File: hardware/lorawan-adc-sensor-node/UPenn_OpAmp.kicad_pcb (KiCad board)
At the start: 2 copper layers, 106 x 147.1 mm, 61 parts, among them J1 643416-1, J2 Conn_02x03_Odd_Even, J3 Conn_01x13_Pin, J4 Conn_01x13_Pin, J5 Conn_02x03_Odd_Even, J6 643416-1, J7 643416-1, SW1 SW_DIP_x03, U1 AD8226, U2 AD8615, U3 ADP7142AUJZ-3.3, U4 AD8226, U5 AD8615, U6 AD8226, U7 AD8615

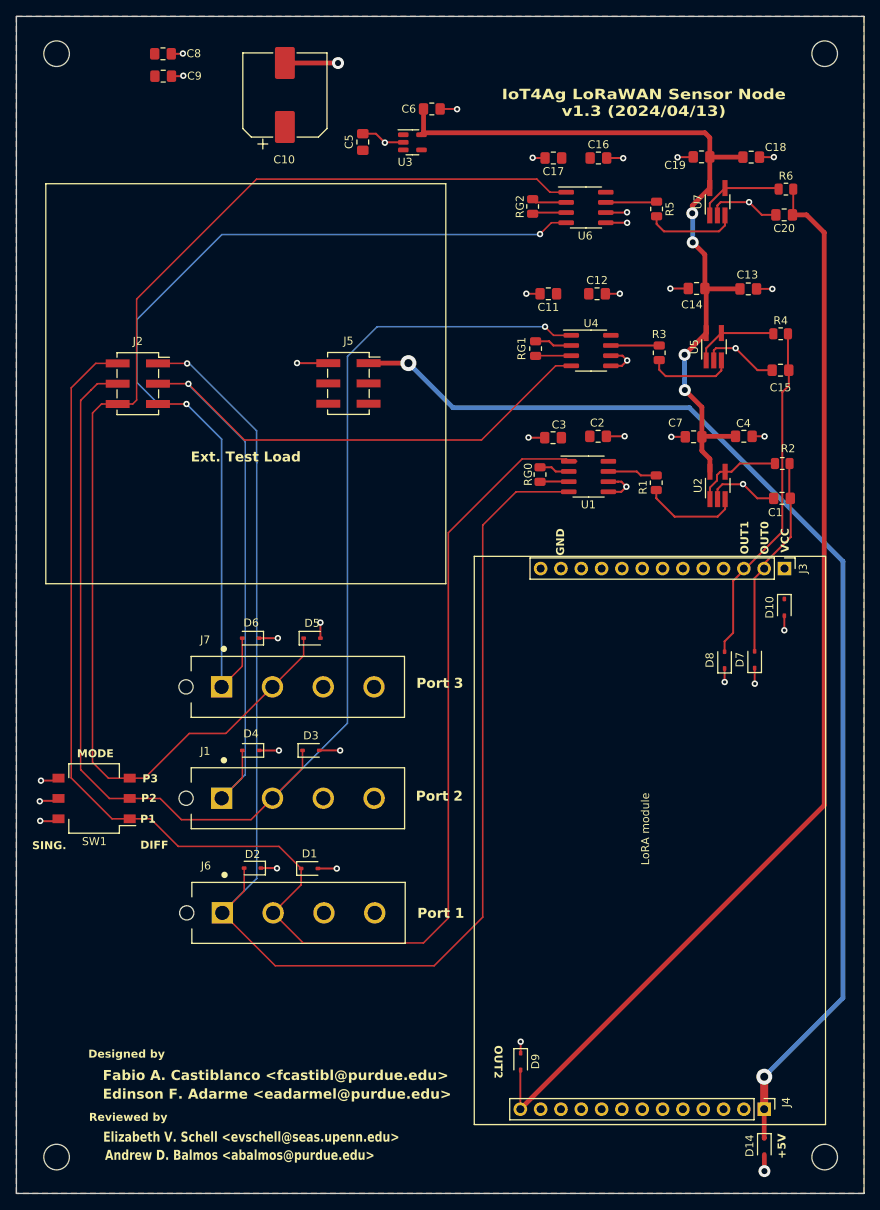
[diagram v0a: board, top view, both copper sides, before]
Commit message: fixed spacing between port connectors and minor layout cosmetic changes
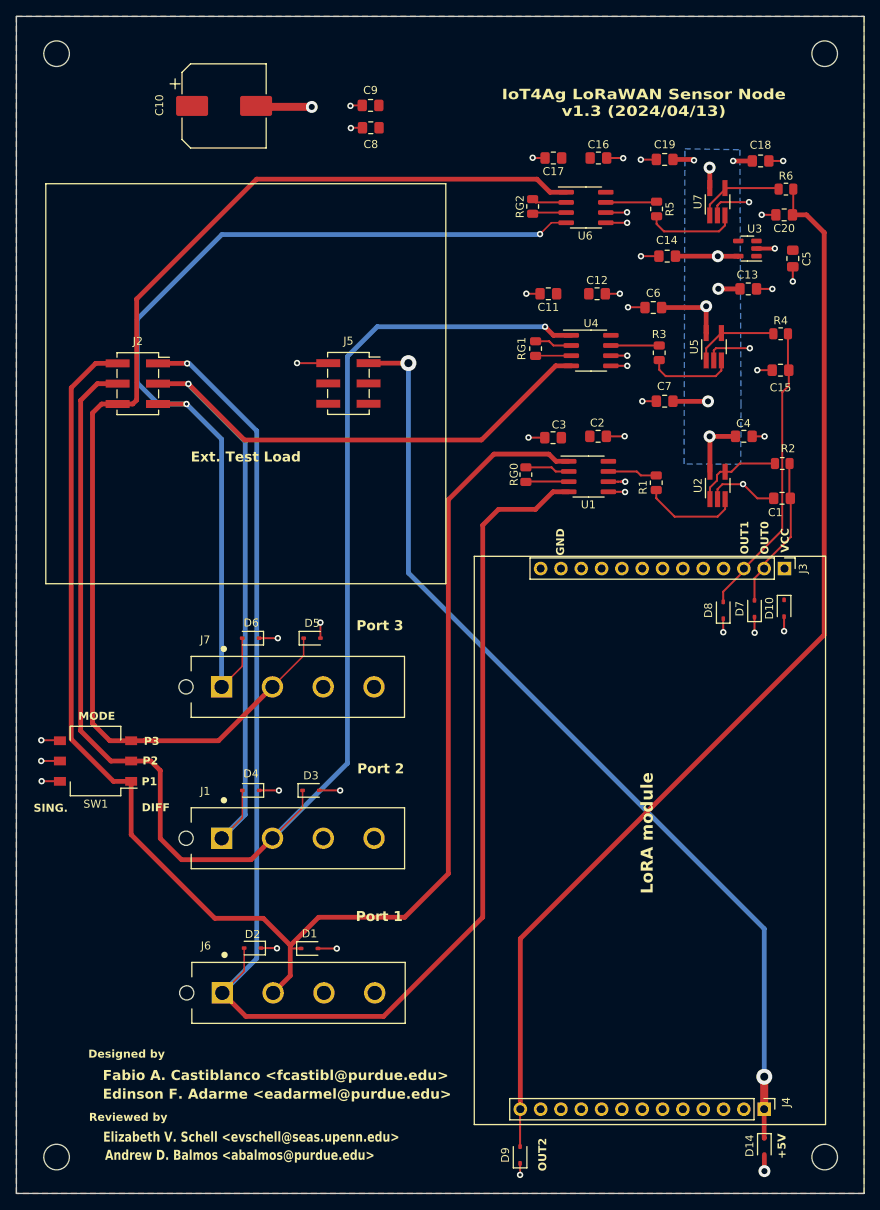
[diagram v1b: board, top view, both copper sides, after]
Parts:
- moved C5 55.7 mm to (149.8, 57.5), turned to 90 degrees
- moved U3 43.9 mm to (144.2, 56.2), turned to 180 degrees
- moved C6 37.2 mm to (132.4, 63.6), turned to 0 degrees
- moved C8 27.6 mm to (97.1, 41.1), turned to 180 degrees
- moved C9 26.2 mm to (97.1, 38.3), turned to 180 degrees
- moved D9 11.7 mm to (115.8, 169.5), turned to 90 degrees
- moved D1 10.0 mm to (89.4, 143.7)
- moved D2 10.0 mm to (82.3, 143.7)
- moved J6 10.0 mm to (88.1, 149.3)
- moved C10 7.72 mm to (78.8, 38.4), turned to 0 degrees
- moved D7 6.37 mm to (145.1, 101.2)
- moved D8 6.22 mm to (141.2, 101.4)
- moved C7 5.74 mm to (133.8, 75.3)
- moved C14 5.46 mm to (134.1, 57.2)
- moved D3 5.00 mm to (89.6, 124.0)
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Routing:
- net /VADC: track 98.3 -> 39.3 mm, vias 4 -> 8
- net /5V_SW: track 145.7 -> 120.3 mm
- net /P1+: track 183.9 -> 195.0 mm
- net /P2-: track 176.0 -> 185.2 mm
- net GND: track 116.8 -> 110.2 mm, vias 39 -> 44
- net /P3-: track 158.8 -> 152.3 mm
- net /P1_OUT: track 25.4 -> 19.1 mm
- net /P2_OUT: track 43.1 -> 37.0 mm
- net /P2+: track 121.5 -> 126.4 mm
- net /RG0-: track 3.59 -> 5.36 mm
- net /RG0+: track 3.81 -> 5.58 mm
- net /P1-: track 189.2 -> 190.2 mm
- added copper zone on B.Cu, net /VADC

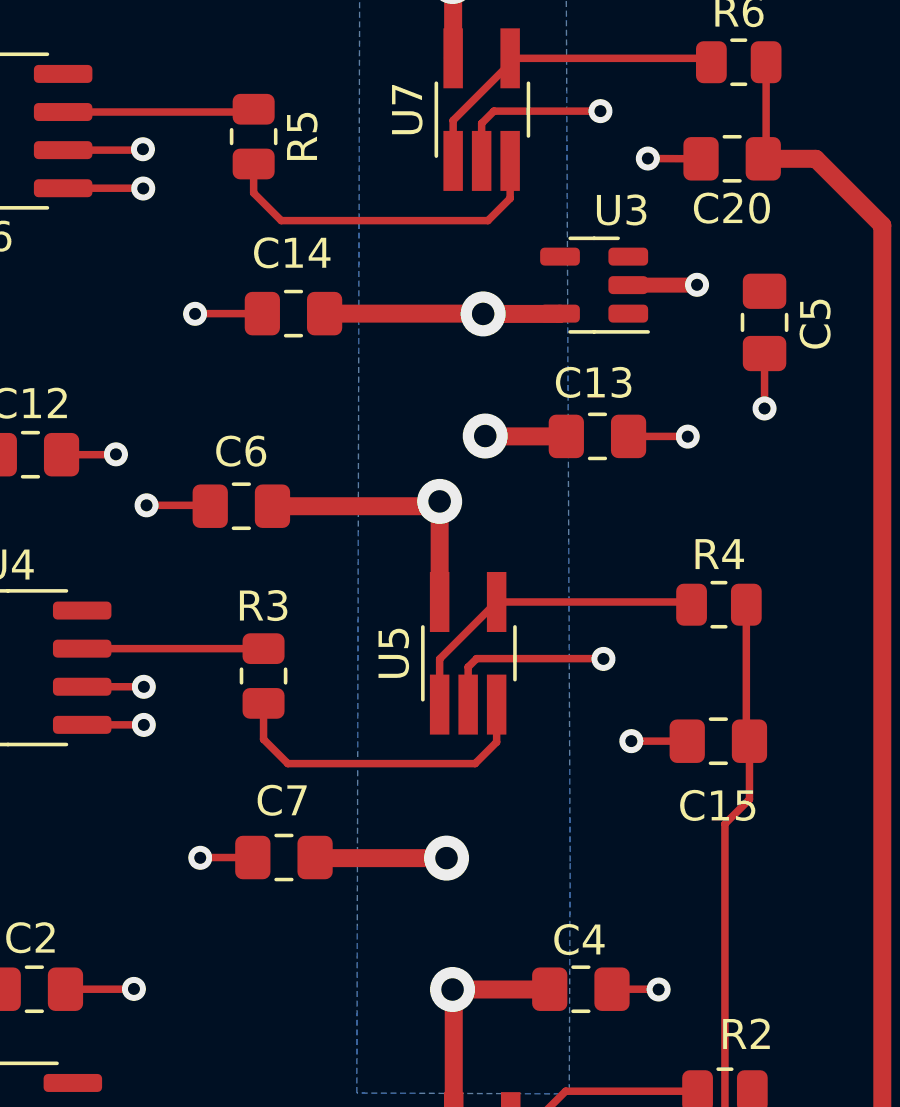
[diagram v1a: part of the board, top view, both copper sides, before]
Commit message: added resistor load test board and adjustments to pulsed current load
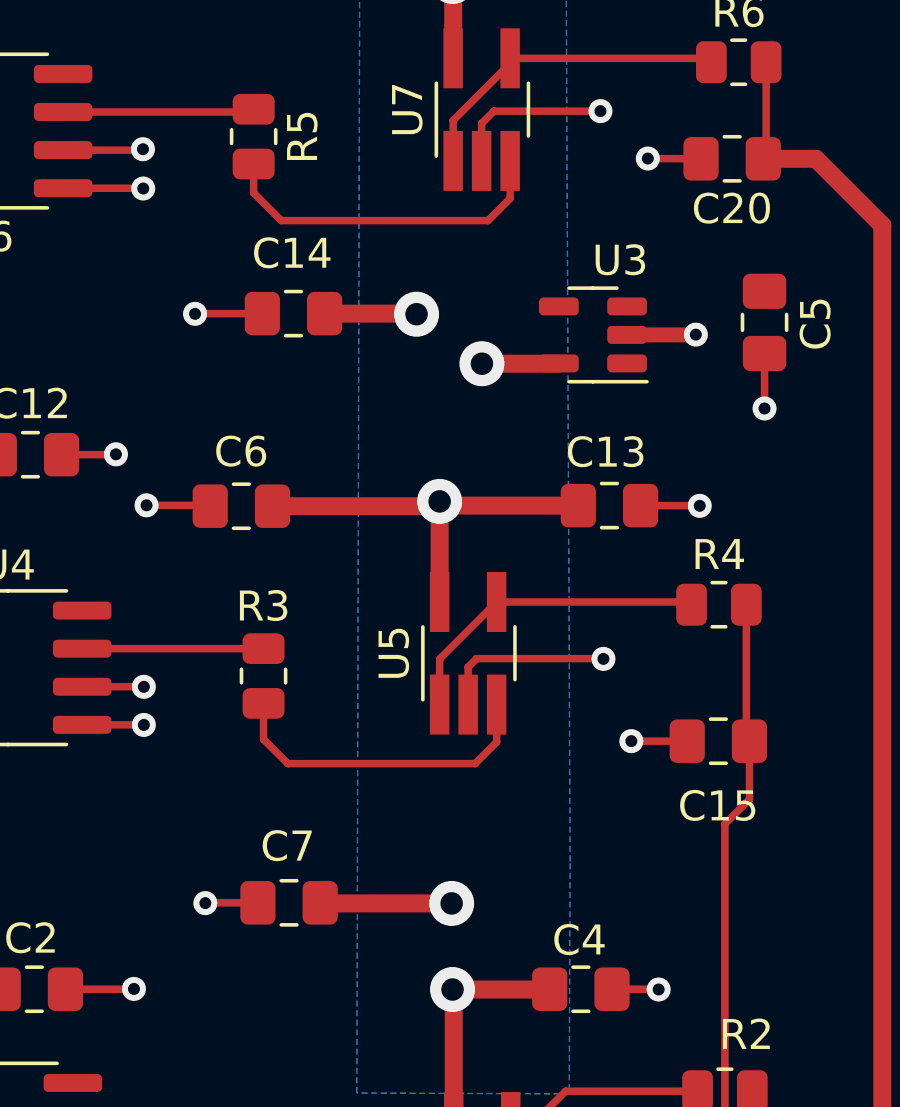
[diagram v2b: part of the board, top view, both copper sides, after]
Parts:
- moved C13 2.34 mm to (144.7, 63.6)
- moved U3 1.66 mm to (144.1, 57.9)
- moved C7 1.52 mm to (134.0, 76.8)
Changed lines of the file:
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@@
 		(tags "capacitor handsolder")
 		(property "Reference" "C6"
-			(at 0 -1.8 360)
+			(at 0 -1.8 0)
 			(layer "F.SilkS")
 			(effects
@@
 		)
 		(property "Value" "1u"
-			(at 0 1.68 360)
+			(at 0 1.68 0)
 			(layer "F.Fab")
 			(effects
@@
 		)
 		(fp_text user "${REFERENCE}"
-			(at 0 0 360)
+			(at 0 0 0)
 			(layer "F.Fab")
 			(effects
@@
 	(footprint "Capacitor_SMD:C_0805_2012Metric_Pad1.18x1.45mm_HandSolder"
 		(layer "F.Cu")
-		(at 133.83 75.3 180)
+		(at 134 76.81 180)
 		(descr "Capacitor SMD 0805 (2012 Metric), square (rectangular) end terminal, IPC_7351 nominal with elongated pad for handsoldering. (Body size source: IPC-SM-782 page 76, https://www.pcb-3d.com/wordpress/wp-content/uploads/ipc-sm-782a_amendment_1_and_2.pdf, https://docs.google.com/spreadsheets/d/1BsfQQcO9C6DZCsRaXUlFlo91Tg2WpOkGARC1WS5S8t0/edit?usp=sharing), generated with kicad-footprint-generator")
 		(tags "capacitor handsolder")
@@
 		(tags "capacitor handsolder")
 		(property "Reference" "C5"
-			(at -0.0375 1.722 270)
+			(at -0.0375 1.722 -90)
 			(layer "F.SilkS")
 			(effects
@@
 		)
 		(property "Value" "1u"
-			(at 0 1.68 270)
+			(at 0 1.68 -90)
 			(layer "F.Fab")
 			(effects
@@
 		)
 		(fp_text user "${REFERENCE}"
-			(at 0 0 270)
+			(at 0 0 -90)
 			(layer "F.Fab")
 			(effects
@@
 		(tags "SOD-323")
 		(property "Reference" "D9"
-			(at 0 -1.85 270)
+			(at 0 -1.85 -90)
 			(layer "F.SilkS")
 			(effects
@@
 		)
 		(property "Value" "ESD9B3.3ST5G"
-			(at 0.1 1.9 270)
+			(at 0.1 1.9 -90)
 			(layer "F.Fab")
 			(effects
@@
 		)
 		(fp_text user "${REFERENCE}"
-			(at 0 -1.85 270)
+			(at 0 -1.85 -90)
 			(layer "F.Fab")
 			(effects
@@
 		)
 		(property "Value" "330u"
-			(at 0 6.2 360)
+			(at 0 6.2 0)
 			(layer "F.Fab")
 			(effects
@@
 		)
 		(fp_text user "${REFERENCE}"
-			(at 0 0 360)
+			(at 0 0 0)
 			(layer "F.Fab")
 			(effects
@@
 	(footprint "Capacitor_SMD:C_0805_2012Metric_Pad1.18x1.45mm_HandSolder"
 		(layer "F.Cu")
-		(at 144.28 61.2625)
+		(at 144.68 63.57)
 		(descr "Capacitor SMD 0805 (2012 Metric), square (rectangular) end terminal, IPC_7351 nominal with elongated pad for handsoldering. (Body size source: IPC-SM-782 page 76, https://www.pcb-3d.com/wordpress/wp-content/uploads/ipc-sm-782a_amendment_1_and_2.pdf, https://docs.google.com/spreadsheets/d/1BsfQQcO9C6DZCsRaXUlFlo91Tg2WpOkGARC1WS5S8t0/edit?usp=sharing), generated with kicad-footprint-generator")
 		(tags "capacitor handsolder")
@@
 	(footprint "Package_TO_SOT_SMD:TSOT-23-5"
 		(layer "F.Cu")
-		(at 144.17 56.22 180)
+		(at 144.13 57.88 180)
 		(descr "TSOT, 5 Pin (https://www.jedec.org/sites/default/files/docs/MO-193D.pdf variant AB), generated with kicad-footprint-generator ipc_gullwing_generator.py")
 		(tags "TSOT TO_SOT_SMD")
@@
 		(tags "capacitor handsolder")
 		(property "Reference" "C18"
-			(at -0.01 -1.99 360)
+			(at -0.01 -1.99 0)
 			(layer "F.SilkS")
 			(effects
@@
 		)
 		(property "Value" "10u"
-			(at 0 1.68 360)
+			(at 0 1.68 0)
 			(layer "F.Fab")
 			(effects
@@
 		)
 		(fp_text user "${REFERENCE}"
-			(at 0 0 360)
+			(at 0 0 0)
 			(layer "F.Fab")
 			(effects
@@
 	)
 	(segment
-		(start 147.59 56.22)
-		(end 147.6 56.21)
-		(width 0.25)
-		(layer "F.Cu")
-		(net 4)
-	)
-	(segment
 		(start 85.605 123.95)
 		(end 85.615 123.96)
@@
 	)
 	(segment
-		(start 145.3075 56.22)
-		(end 147.59 56.22)
+		(start 145.2675 57.88)
+		(end 147.55 57.88)
 		(width 0.5)
 		(layer "F.Cu")
@@
 	)
 	(segment
-		(start 147.2825 61.2625)
-		(end 147.29 61.27)
-		(width 0.25)
-		(layer "F.Cu")
-		(net 4)
-	)
-	(segment
 		(start 147.27 71.42)
 		(end 147.2725 71.4225)
@@
 	)
 	(segment
-		(start 132.7925 75.3)
-		(end 131.05 75.3)
+		(start 132.9625 76.81)
+		(end 131.22 76.81)
 		(width 0.25)
 		(layer "F.Cu")
@@
 	)
 	(segment
-		(start 145.3175 61.2625)
-		(end 147.2825 61.2625)
+		(start 145.7175 63.57)
+		(end 147.6825 63.57)
 		(width 0.25)
 		(layer "F.Cu")
@@
 	)
 	(via
-		(at 147.6 56.21)
+		(at 147.56 57.87)
 		(size 0.8)
 		(drill 0.4)
@@
 	)
 	(via
-		(at 131.04 75.31)
+		(at 131.21 76.82)
 		(size 0.8)
 		(drill 0.4)
@@
 	)
 	(via
-		(at 147.29 61.27)
+		(at 147.69 63.5775)
 		(size 0.8)
 		(drill 0.4)
@@
 	)
 	(segment
-		(start 143.2425 61.2625)
-		(end 140.5525 61.2625)
-		(width 0.6)
-		(layer "F.Cu")
-		(net 6)
-	)
-	(segment
 		(start 138.86 63.59)
 		(end 139.02 63.43)
@@
 	)
 	(segment
-		(start 140.5525 61.2625)
-		(end 140.54 61.25)
-		(width 0.6)
-		(layer "F.Cu")
-		(net 6)
-	)
-	(segment
-		(start 140.47 57.18)
-		(end 143.0225 57.18)
+		(start 140.43 58.84)
+		(end 142.9825 58.84)
 		(width 0.6)
 		(layer "F.Cu")
@@
 	)
 	(segment
-		(start 135.185 57.17)
-		(end 140.46 57.17)
+		(start 139.47 48.66)
+		(end 139.46 48.65)
 		(width 0.6)
 		(layer "F.Cu")
@@
 	)
 	(segment
-		(start 139.47 48.66)
-		(end 139.46 48.65)
+		(start 143.6425 63.57)
+		(end 139.16 63.57)
 		(width 0.6)
 		(layer "F.Cu")
@@
 	)
 	(segment
-		(start 143.0225 57.18)
-		(end 143.0325 57.17)
-		(width 0.6)
-		(layer "F.Cu")
-		(net 6)
-	)
-	(segment
-		(start 140.46 57.17)
-		(end 140.47 57.18)
+		(start 139.16 63.57)
+		(end 139.02 63.43)
 		(width 0.6)
 		(layer "F.Cu")
@@
 	)
 	(segment
-		(start 134.8875 75.32)
-		(end 134.8675 75.3)
+		(start 135.0575 76.83)
+		(end 135.0375 76.81)
+		(width 0.6)
+		(layer "F.Cu")
+		(net 6)
+	)
+	(segment
+		(start 135.185 57.17)
+		(end 138.23 57.17)
+		(width 0.6)
+		(layer "F.Cu")
+		(net 6)
+	)
+	(segment
+		(start 138.23 57.17)
+		(end 138.25 57.19)
 		(width 0.6)
 		(layer "F.Cu")
@@
 	)
 	(segment
-		(start 139.25 75.32)
-		(end 134.8875 75.32)
+		(start 139.42 76.83)
+		(end 135.0575 76.83)
 		(width 0.6)
 		(layer "F.Cu")
@@
 	)
 	(via
-		(at 140.54 61.25)
+		(at 138.25 57.19)
 		(size 1.5)
 		(drill 0.75)
@@
 	)
 	(via
-		(at 140.47 57.18)
+		(at 140.43 58.84)
 		(size 1.5)
 		(drill 0.75)
@@
 	)
 	(via
-		(at 139.25 75.32)
+		(at 139.42 76.83)
 		(size 1.5)
 		(drill 0.75)
